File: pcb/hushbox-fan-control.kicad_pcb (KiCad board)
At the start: 2 copper layers, 57.1 x 53.3 mm, 23 parts, among them J1 Barrel_Jack_MountingPin, J2 Conn_01x15_Male, M1 Fan_Tacho_PWM, M2 Fan_Tacho_PWM, Q1 IRLML2520, Q2 IRLML2520, SW1 SW_SPST, U1 AMS1117-3.3, U2 ESP32-DevKit-V1, U3 DS18B20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

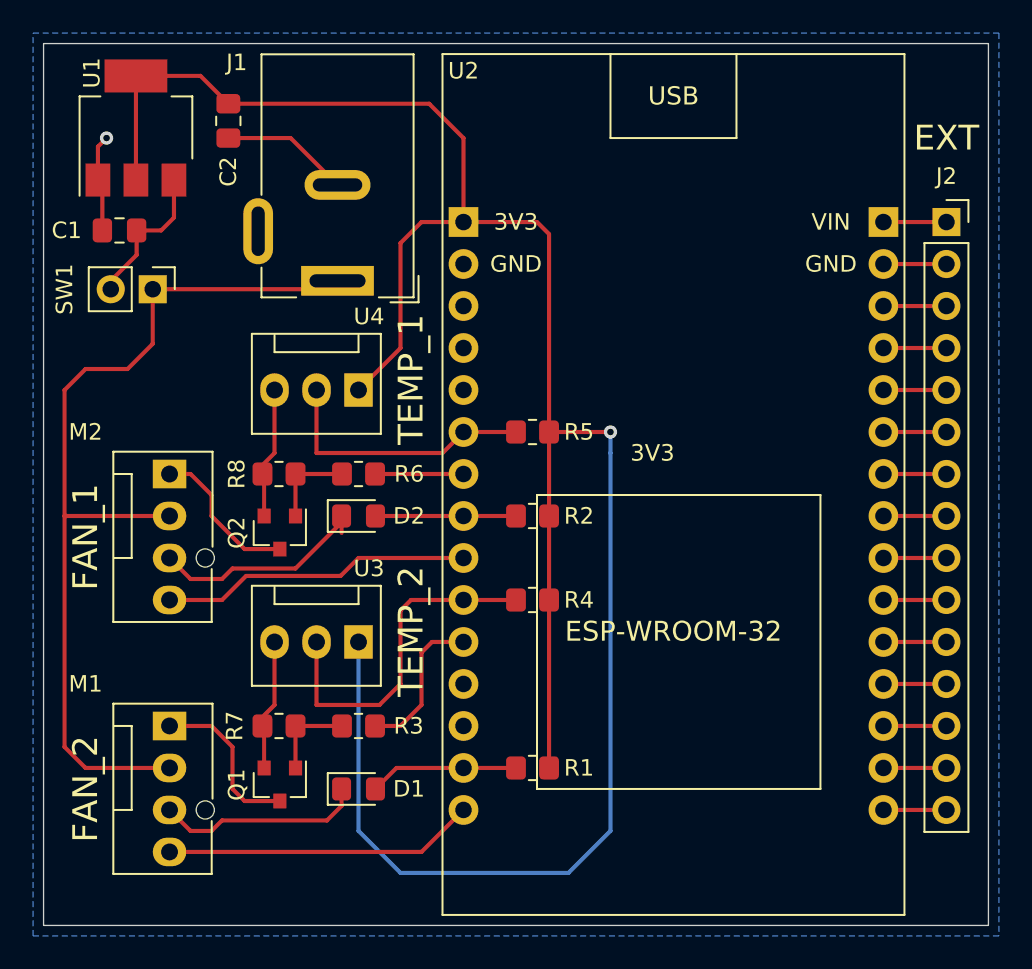
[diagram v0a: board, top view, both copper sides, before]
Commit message: improve pcb to v1.1 with IR support
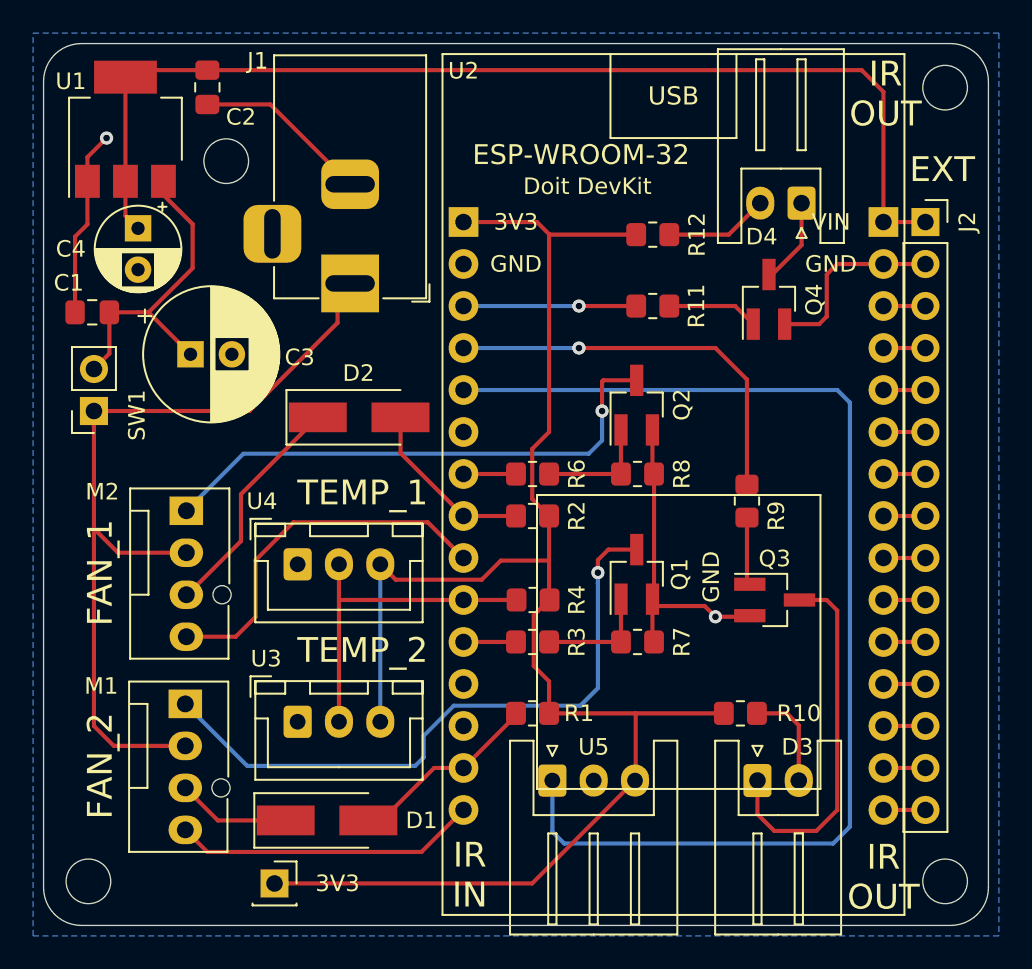
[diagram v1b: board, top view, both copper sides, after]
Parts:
- removed R5: R, Resistor_SMD:R_0805_2012Metric_Pad1.20x1.40mm_HandSolder
- added 3V3: PinSocket_1x01_P2.54mm_Vertical, Connector_PinSocket_2.54mm:PinSocket_1x01_P2.54mm_Vertical, F.Cu at (118.1, 113.7)
- added C3: 100u, Capacitor_THT:CP_Radial_D8.0mm_P2.50mm, F.Cu at (113.0, 81.7)
- added C4: 10u, Capacitor_THT:CP_Radial_D5.0mm_P2.50mm, F.Cu at (109.9, 74.0)
- added D3: LD271, Connector_JST:JST_XH_S2B-XH-A_1x02_P2.50mm_Horizontal, F.Cu at (147.3, 107.4)
- added D4: LD271, Connector_JST:JST_XH_S2B-XH-A_1x02_P2.50mm_Horizontal, F.Cu at (150.0, 72.5)
- added Q3: MMBT3904, Package_TO_SOT_SMD:SOT-23_Handsoldering, F.Cu at (148.4, 96.5)
- added Q4: MMBT3904, Package_TO_SOT_SMD:SOT-23_Handsoldering, F.Cu at (148.0, 78.3)
- added R10: 20, Resistor_SMD:R_0805_2012Metric_Pad1.20x1.40mm_HandSolder, F.Cu at (146.3, 103.4)
- added R11: 330, Resistor_SMD:R_0805_2012Metric_Pad1.20x1.40mm_HandSolder, F.Cu at (141.0, 78.7)
- added R12: 20, Resistor_SMD:R_0805_2012Metric_Pad1.20x1.40mm_HandSolder, F.Cu at (141.0, 74.4)
- added R9: 330, Resistor_SMD:R_0805_2012Metric_Pad1.20x1.40mm_HandSolder, F.Cu at (146.7, 90.5)
- added U5: TSDP341xx, Connector_JST:JST_XH_S3B-XH-A_1x03_P2.50mm_Horizontal, F.Cu at (134.9, 107.4)
- C1, C2: value C -> 100n
- D1, D2: value D -> 1N4001; footprint Diode_SMD:D_0805_2012Metric_Pad1.15x1.40mm_HandSolder -> Diode_SMD:D_SMA_Handsoldering
- J1: footprint Connector_BarrelJack:BarrelJack_Wuerth_6941xx301002 -> Connector_BarrelJack:BarrelJack_Horizontal
- Q1, Q2: value IRLML2520 -> IRLML2502; footprint Package_TO_SOT_SMD:SOT-23 -> Package_TO_SOT_SMD:SOT-23_Handsoldering
- R1, R2: value R -> 4.7k
- R3, R6: value R -> 100
- R4: value R -> 1k
- R7, R8: value R -> 10k
- SW1: footprint Connector_PinHeader_2.54mm:PinHeader_1x02_P2.54mm_Vertical -> Connector_PinSocket_2.54mm:PinSocket_1x02_P2.54mm_Vertical
- U1: value AMS1117-3.3 -> AMS1117-5.0
- U3, U4: footprint Connector:FanPinHeader_1x03_P2.54mm_Vertical -> Connector_JST:JST_XH_B3B-XH-A_1x03_P2.50mm_Vertical
- moved Q1 25.1 mm to (140.0, 95.0), turned to 90 degrees
- moved Q2 22.9 mm to (140.0, 84.7), turned to 90 degrees
- moved R7 22.3 mm to (140.1, 99.1), turned to 0 degrees
- moved R8 21.7 mm to (140.1, 88.9), turned to 0 degrees
- moved R3 11.7 mm to (133.7, 99.1), turned to 180 degrees
- moved U4 11.2 mm to (119.5, 94.4), turned to 0 degrees
- moved R6 10.5 mm to (133.7, 88.9), turned to 180 degrees
- moved SW1 8.18 mm to (107.2, 85.1), turned to 180 degrees
- moved U3 6.07 mm to (119.5, 103.9), turned to 0 degrees
- moved D2 5.97 mm to (123.2, 85.5)
- moved C1 5.22 mm to (107.1, 79.1)
- moved R1 3.30 mm to (133.7, 103.4)
- moved D1 2.69 mm to (121.3, 109.9)
- moved M2 2.44 mm to (112.8, 91.1)
- moved C2 2.40 mm to (114.0, 65.5)
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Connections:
- C2 pad 1: +3V3 -> +5V
- J2 pad 1: Net-(J2-Pad1) -> +5V
- R4 pad 1: +3V3 -> Net-(R4-Pad1)
- R4 pad 2: Net-(R4-Pad2) -> +3V3
- U1 pad 2: +3V3 -> +5V
- U2 pad 1: Net-(J2-Pad1) -> +5V
- U2 pad 21: Net-(R5-Pad2) -> Net-(U2-Pad21)
- U2 pad 25: Net-(R4-Pad2) -> Net-(R4-Pad1)
- U3 pad 1: +3V3 -> GND
- U3 pad 2: Net-(R4-Pad2) -> Net-(R4-Pad1)
- U3 pad 3: GND -> +3V3
- U4 pad 1: +3V3 -> GND
- U4 pad 2: Net-(R5-Pad2) -> Net-(R4-Pad1)
- U4 pad 3: GND -> +3V3
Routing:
- net Net-(U2-Pad20): track 0.00 -> 71.2 mm
- net +5V: track 0.00 -> 67.1 mm
- net +3V3: track 141.4 -> 101.0 mm, vias 1 -> 0
- net Net-(M1-Pad1): track 10.0 -> 39.6 mm, vias 0 -> 1
- net Net-(R9-Pad1): track 0.00 -> 24.3 mm, vias 0 -> 1
- net Net-(M2-Pad1): track 9.51 -> 32.6 mm, vias 0 -> 1
- net Net-(D3-Pad1): track 0.00 -> 22.4 mm
- net Net-(R4-Pad2): track 21.1 -> 0.00 mm
- net Net-(R4-Pad1): track 0.00 -> 20.2 mm
- net GND: track 33.6 -> 52.6 mm, vias 1 -> 2
- net Net-(R5-Pad2): track 16.4 -> 0.00 mm
- net Net-(C1-Pad1): track 9.06 -> 19.5 mm
- net Net-(R11-Pad1): track 0.00 -> 10.4 mm, vias 0 -> 1
- net Net-(D4-Pad2): track 0.00 -> 6.29 mm
- net Net-(D3-Pad2): track 0.00 -> 6.17 mm
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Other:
- outline, holes or cut-outs redrawn
- board text added: "Doit DevKit"
- board text added: "Hushbox Control v1.1"
- board text added: "IR IN"
- board text added: "IR OUT"
- board text removed: "3V3"
- board text removed: "Hushbox Fan Control v1.0"
